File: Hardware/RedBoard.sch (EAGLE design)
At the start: 68 parts, among them IC3 LM1117, J1 AMP FCI 10103594-0001LF, J2 ISP, J3 POWER_JACKSUPER_BOMB_DIGITY, Q1 1A/60V/500mΩ, Q2 2N7002PW, Q3 2N7002PW, U1 CH340C, U3 AP2112-3.3V, U4 ATMEGA328P_TQFP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

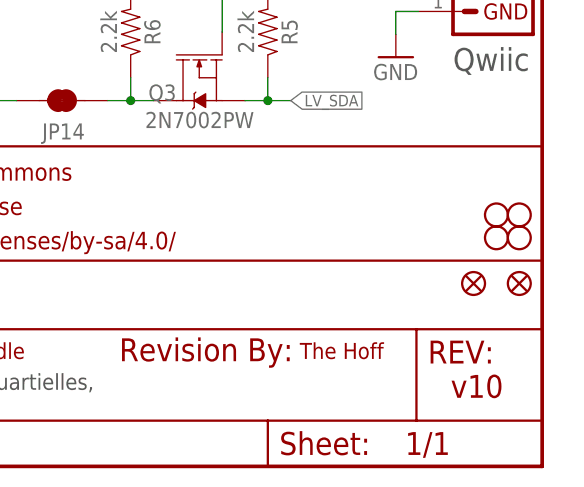
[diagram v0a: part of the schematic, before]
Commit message: Post Checklist changes
Addressed polarity opin markings, documentation items like revised by.
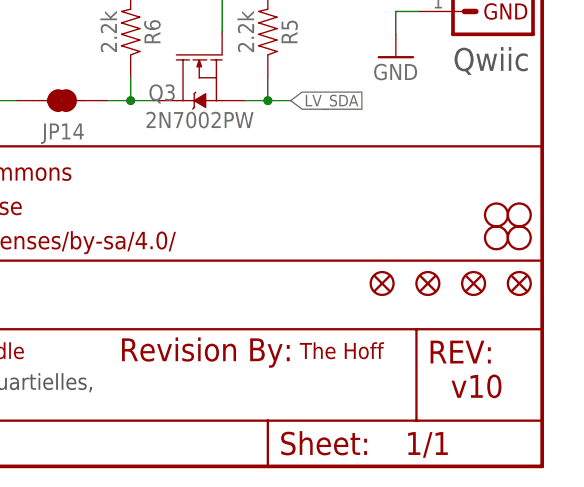
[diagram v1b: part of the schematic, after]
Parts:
- added JP15, JP16: FIDUCIAL1X2, SparkFun:FIDUCIAL1X2
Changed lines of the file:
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@@
 <part name="JP14" library="SparkFun-Jumpers" deviceset="JUMPER-SMT_2_NC_TRACE" device="_SILK" value=""/>
 <part name="LOGO1" library="SparkFun-Aesthetics" deviceset="REVISION" device=""/>
+<part name="JP15" library="SparkFun" deviceset="FIDUCIAL" device="1X2"/>
+<part name="JP16" library="SparkFun" deviceset="FIDUCIAL" device="1X2"/>
 </parts>
 <sheets>
@@
 <instance part="JP14" gate="G$1" x="195.58" y="40.64" rot="R180"/>
 <instance part="LOGO1" gate="G$1" x="201.93" y="11.684"/>
+<instance part="JP15" gate="G$1" x="236.22" y="20.32" rot="R90"/>
+<instance part="JP16" gate="G$1" x="231.14" y="20.32" rot="R90"/>
 </instances>
 <busses>

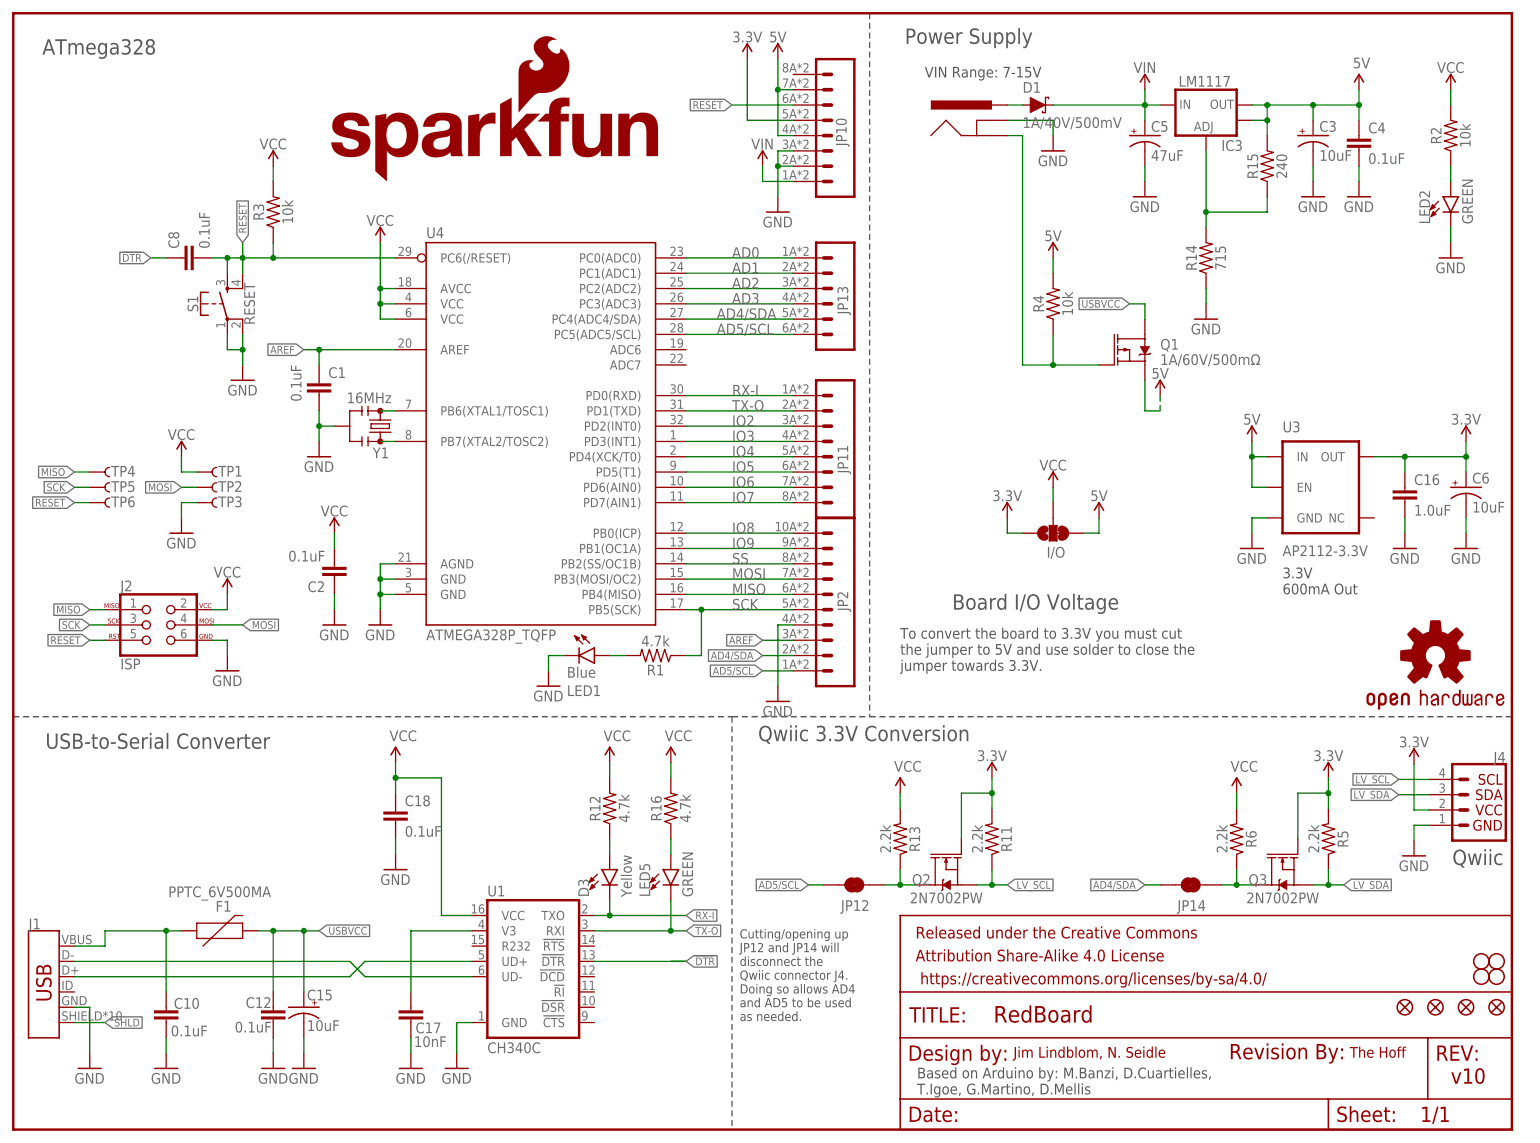
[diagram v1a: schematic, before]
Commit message: Redboard Qwiic Bom/Package Update
Several outdated packages were present in design. Packages updated and bom updated.
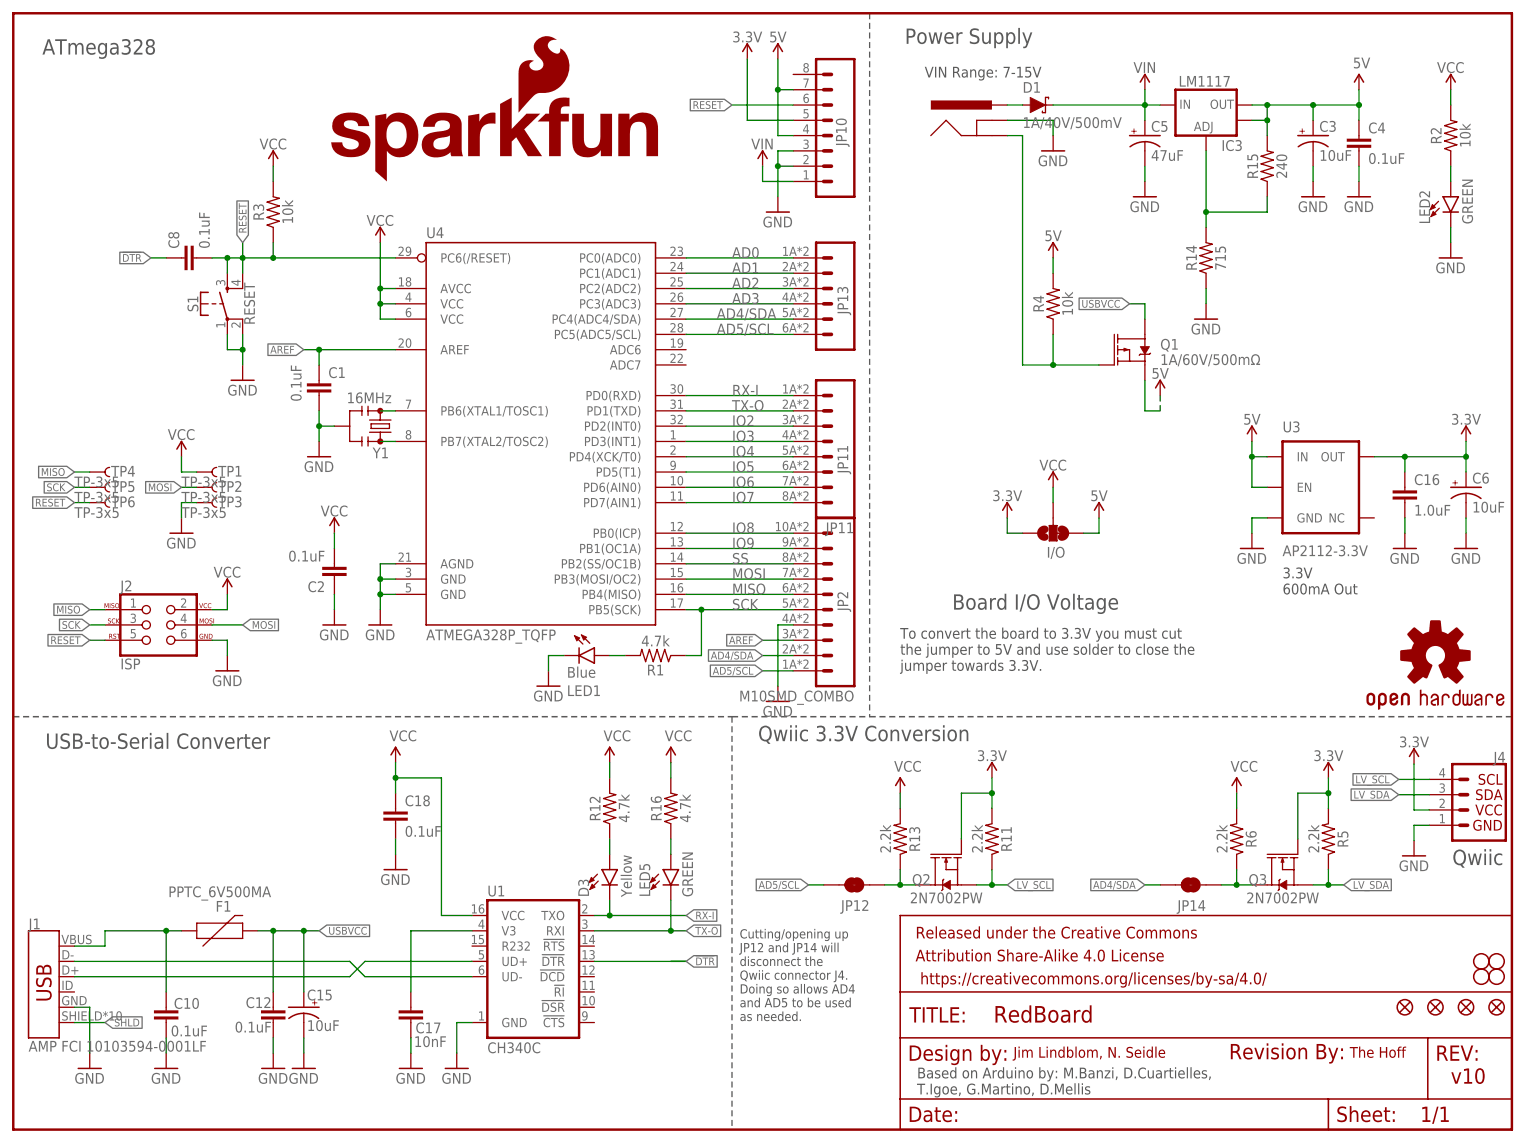
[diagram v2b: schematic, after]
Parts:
- C18: device SparkFun-Capacitors:0.1UF-25V(+80/-20%)(0603) -> SparkFun-Capacitors:0.1UF-0603-25V-(+80/-20%)
- JP10: device SparkFun-Connectors:M08SMD-COMBO -> SparkFun-Connectors:CONN_08SMD-COMBO-FEMALE
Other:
- moved on the sheet: JP10

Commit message: Updated Green TX LED Prod ID
Updated LED5 to Green TX LED Prod ID.
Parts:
- LED5: device SparkFun-LED:LED-GREEN_HIDDENSILK -> SparkFun-LED:LED-GREENLILYPAD
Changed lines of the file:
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@@
 <?xml version="1.0" encoding="utf-8"?>
 <!DOCTYPE eagle SYSTEM "eagle.dtd">
-<eagle version="9.2.0">
+<eagle version="9.1.3">
 <drawing>
 <settings>
@@
 <part name="R16" library="SparkFun-Resistors" deviceset="4.7KOHM" device="-0603-1/10W-1%" value="4.7k"/>
 <part name="J1" library="SparkFun-Connectors" deviceset="USB_MICRO-B" device="_HALF_PTH_MILL" value="AMP FCI 10103594-0001LF"/>
-<part name="LED5" library="SparkFun-LED" deviceset="LED-GREEN" device="_HIDDENSILK" value="GREEN"/>
+<part name="LED5" library="SparkFun-LED" deviceset="LED-GREEN" device="LILYPAD" value="GREEN"/>
 <part name="SUPPLY14" library="SparkFun-PowerSymbols" deviceset="VCC" device=""/>
 <part name="SUPPLY13" library="SparkFun-PowerSymbols" deviceset="VCC" device=""/>

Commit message: Revert "Updated Prod ID of Green LED"
This reverts commit 7f3e58299cb6063360d5b40b06a29a7e7771cac4.
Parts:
- LED5: device SparkFun-LED:LED-GREENLILYPAD -> SparkFun-LED:LED-GREEN_HIDDENSILK
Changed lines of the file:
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@@
 <?xml version="1.0" encoding="utf-8"?>
 <!DOCTYPE eagle SYSTEM "eagle.dtd">
-<eagle version="9.1.3">
+<eagle version="9.2.0">
 <drawing>
 <settings>
@@
 <part name="R16" library="SparkFun-Resistors" deviceset="4.7KOHM" device="-0603-1/10W-1%" value="4.7k"/>
 <part name="J1" library="SparkFun-Connectors" deviceset="USB_MICRO-B" device="_HALF_PTH_MILL" value="AMP FCI 10103594-0001LF"/>
-<part name="LED5" library="SparkFun-LED" deviceset="LED-GREEN" device="LILYPAD" value="GREEN"/>
+<part name="LED5" library="SparkFun-LED" deviceset="LED-GREEN" device="_HIDDENSILK" value="GREEN"/>
 <part name="SUPPLY14" library="SparkFun-PowerSymbols" deviceset="VCC" device=""/>
 <part name="SUPPLY13" library="SparkFun-PowerSymbols" deviceset="VCC" device=""/>
